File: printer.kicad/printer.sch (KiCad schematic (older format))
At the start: 35 parts, among them J1 ZX_Spectrum_128K_expansion, J2 Conn_01x08_Male, J3 Conn_01x05_Male, J4 Conn_01x04_Male, U1 SN74AHC373, U2 SN74HCT00, U3 SN74AHCT02, U4 SN74AHC373, U5 XC6206PxxxMR, U6 STM32F103C8Tx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

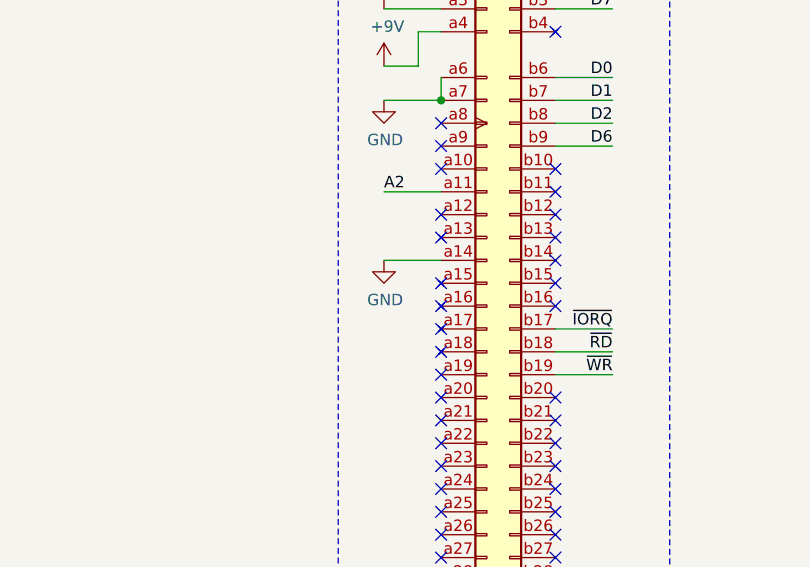
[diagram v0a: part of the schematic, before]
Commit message: Do not connect to the separate ground pin on the bus
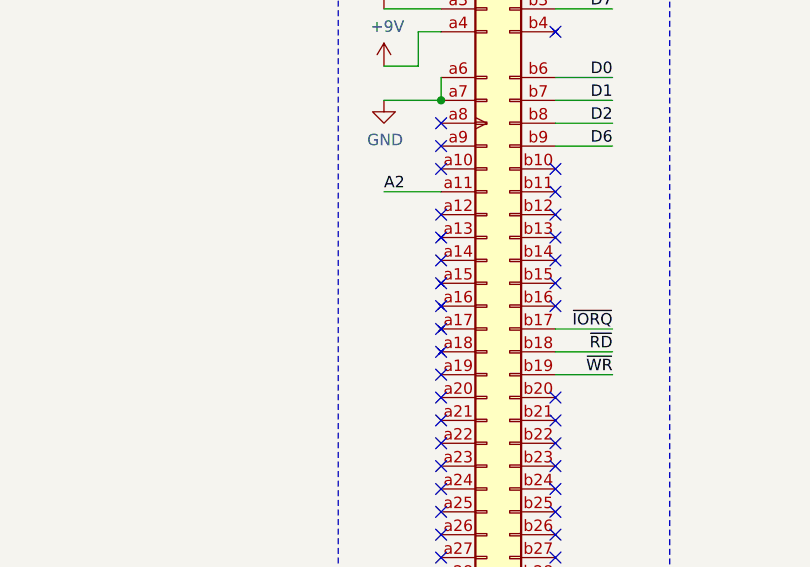
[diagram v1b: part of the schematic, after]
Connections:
- wire segments 145 -> 144
- no-connect marks 68 -> 69
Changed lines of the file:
@@
 	800  1700 1050 1700
-$Comp
-L power:GND #PWR05
-U 1 1 5E1E0363
-P 800 2400
-F 0 "#PWR05" H 800 2150 50  0001 C CNN
-F 1 "GND" H 805 2227 50  0000 C CNN
-F 2 "" H 800 2400 50  0001 C CNN
-F 3 "" H 800 2400 50  0001 C CNN
-	1    800  2400
-	1    0    0    -1
-$EndComp
-Wire Wire Line
-	800  2400 1050 2400
 $Comp
 L power:PWR_FLAG #FLG01
@@
 	1    0    0    -1
 $EndComp
+NoConn ~ 1050 2400
 $EndSCHEMATC

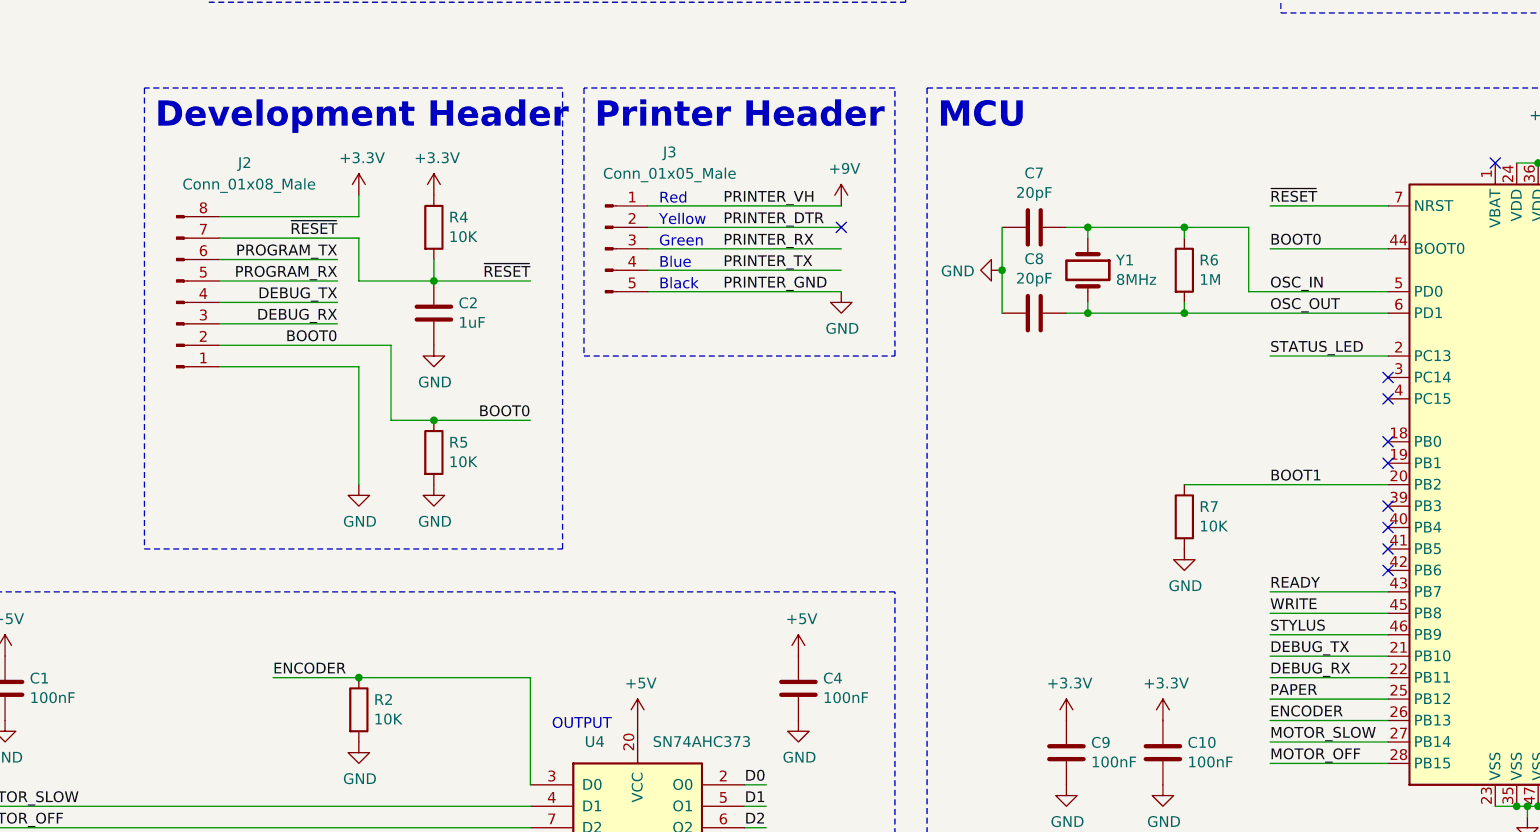
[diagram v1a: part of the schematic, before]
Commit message: Remove debug serial
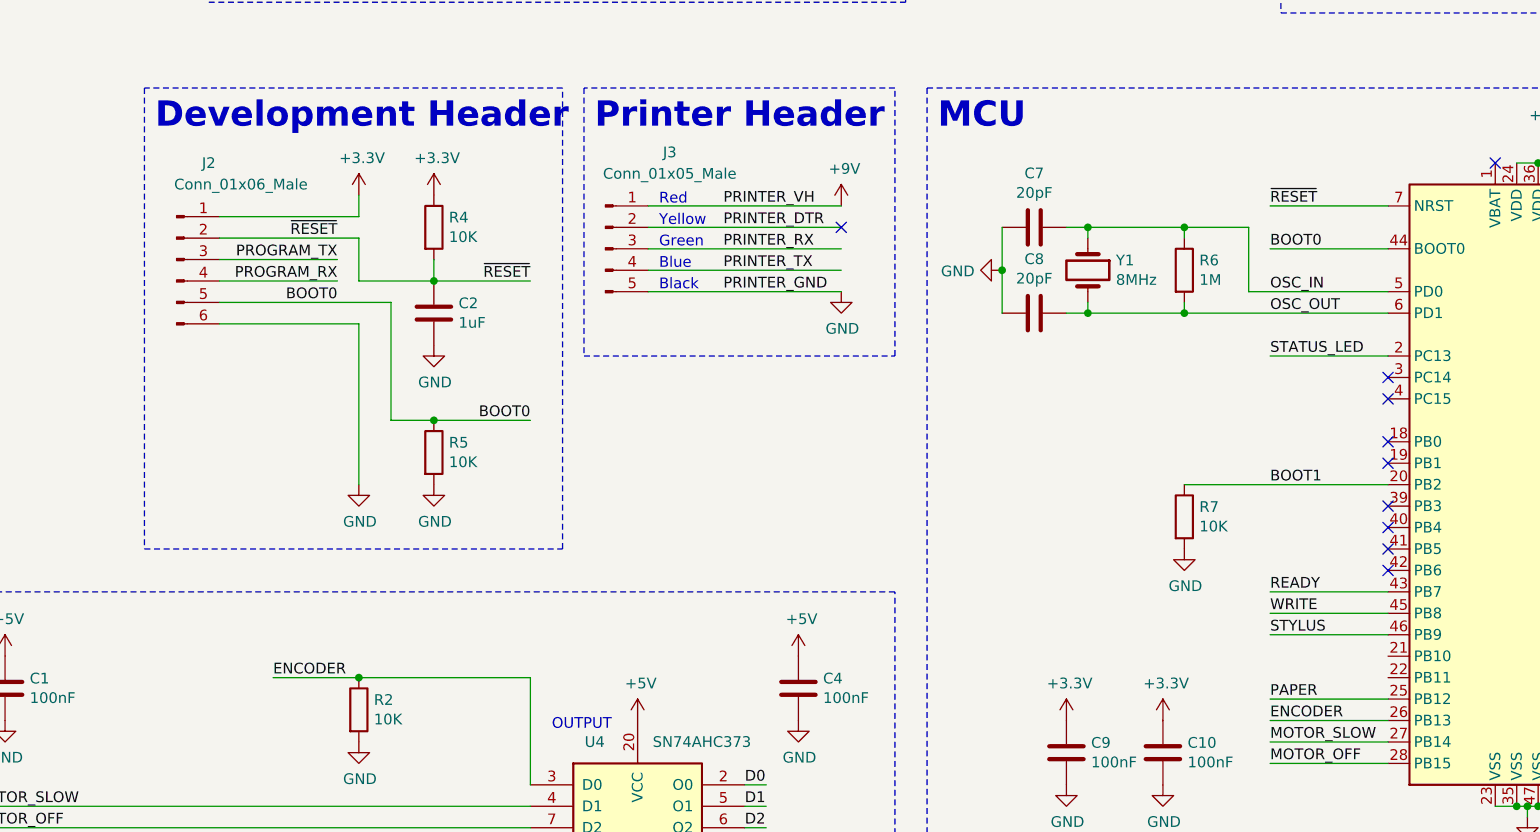
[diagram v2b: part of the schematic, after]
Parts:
- removed J2: Conn_01x08_Male, Connector_PinHeader_2.54mm:PinHeader_1x08_P2.54mm_Vertical, symbol Connector:Conn_01x08_Male
- added J2: Conn_01x06_Male, Connector_PinHeader_2.54mm:PinHeader_1x06_P2.54mm_Vertical, symbol Connector:Conn_01x06_Male
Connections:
- net labels removed: DEBUG_RX, DEBUG_TX
- wire segments 144 -> 140
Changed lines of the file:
@@
 Wire Wire Line
 	4700 5000 4700 5500
-Text Label 8150 4900 0    50   ~ 0
-DEBUG_TX
-Text Label 8150 5000 0    50   ~ 0
-DEBUG_RX
 Text Label 8150 4700 0    50   ~ 0
 WRITE
@@
 MOTOR_OFF
 Wire Wire Line
-	8150 4900 8700 4900
-Wire Wire Line
-	8150 5000 8700 5000
-Wire Wire Line
 	8150 4700 8700 4700
 Wire Wire Line
@@
 	3250 2850 3900 2850
 Wire Wire Line
-	3900 4100 3900 3550
-Wire Wire Line
 	4250 3050 4250 3150
 $Comp
@@
 	1    0    0    -1
 $EndComp
-Wire Wire Line
-	3250 3550 3900 3550
 Text Label 3800 3050 2    50   ~ 0
 PROGRAM_TX
@@
 Text Notes 6600 800  0    118  ~ 24
 MCU Power
-$Comp
-L Connector:Conn_01x08_Male J2
-U 1 1 5E996EA0
-P 3050 3250
-F 0 "J2" H 3400 2600 50  0000 R CNN
-F 1 "Conn_01x08_Male" H 3700 2700 50  0000 R CNN
-F 2 "Connector_PinHeader_2.54mm:PinHeader_1x08_P2.54mm_Vertical" H 3050 3250 50  0001 C CNN
-F 3 "~" H 3050 3250 50  0001 C CNN
-	1    3050 3250
-	1    0    0    1
-$EndComp
 Wire Wire Line
 	3900 2850 3900 2750
@@
 	3900 2950 3900 3150
 Wire Wire Line
-	4050 3800 4050 3450
-Wire Wire Line
-	4050 3450 3250 3450
-Wire Wire Line
 	3900 3150 4250 3150
 Connection ~ 4250 3150
@@
 Text Label 8150 3500 0    50   ~ 0
 STATUS_LED
-Text Label 3800 3450 2    50   ~ 0
-BOOT0
 Text Label 3800 2950 2    50   ~ 0
 ~RESET
@@
 Wire Wire Line
 	10250 1150 10800 1150
-Text Label 3800 3250 2    50   ~ 0
-DEBUG_TX
-Text Label 3800 3350 2    50   ~ 0
-DEBUG_RX
-Wire Wire Line
-	3800 3350 3250 3350
-Wire Wire Line
-	3800 3250 3250 3250
 Wire Notes Line width 10
 	9900 1750 11100 1750
@@
 $EndComp
 NoConn ~ 1050 2400
+$Comp
+L Connector:Conn_01x06_Male J2
+U 1 1 5E08EF06
+P 3050 3050
+F 0 "J2" H 3200 3500 50  0000 C CNN
+F 1 "Conn_01x06_Male" H 3350 3400 50  0000 C CNN
+F 2 "Connector_PinHeader_2.54mm:PinHeader_1x06_P2.54mm_Vertical" H 3050 3050 50  0001 C CNN
+F 3 "~" H 3050 3050 50  0001 C CNN
+	1    3050 3050
+	1    0    0    -1
+$EndComp
+Wire Wire Line
+	4050 3800 4050 3250
+Wire Wire Line
+	4050 3250 3250 3250
+Text Label 3800 3250 2    50   ~ 0
+BOOT0
+Wire Wire Line
+	3900 4100 3900 3350
+Wire Wire Line
+	3250 3350 3900 3350
 $EndSCHEMATC

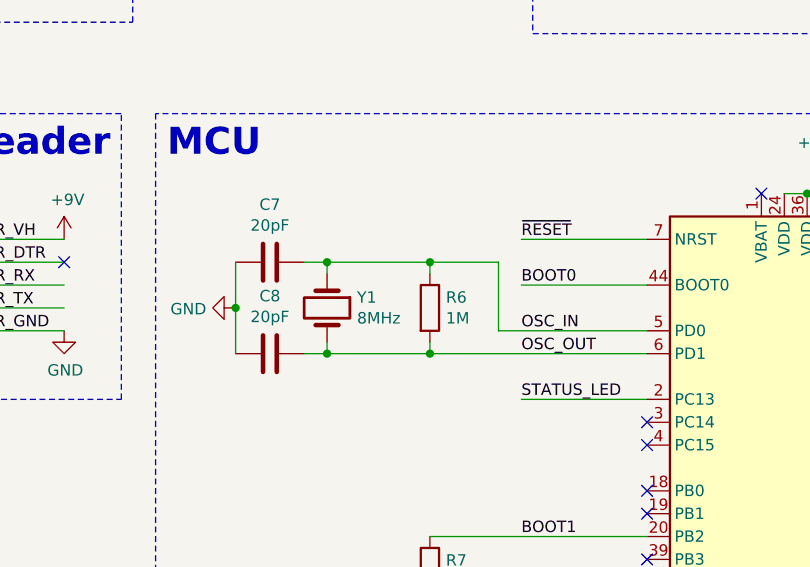
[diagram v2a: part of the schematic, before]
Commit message: Remove oscillator load resistor
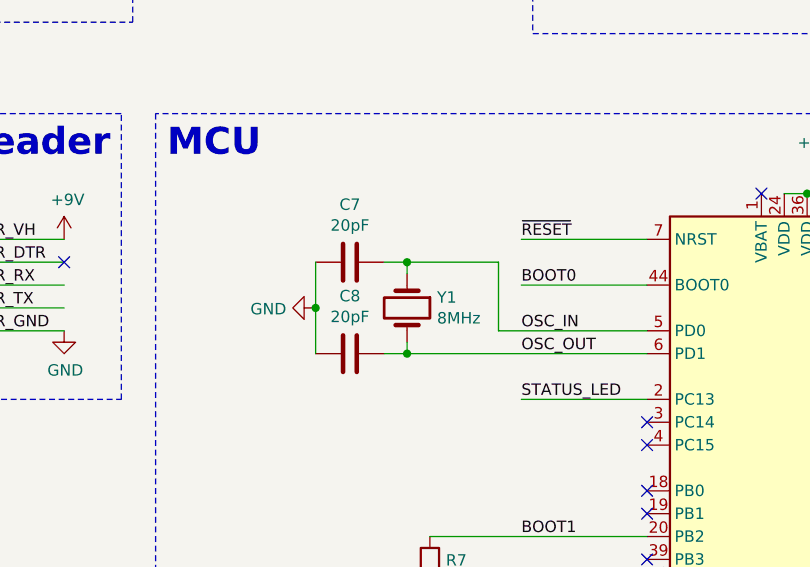
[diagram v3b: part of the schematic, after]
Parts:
- removed R6: 1M, Resistor_SMD:R_0603_1608Metric, symbol Device:R
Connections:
- wire segments 140 -> 136
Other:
- moved on the sheet: C7, C8, Y1
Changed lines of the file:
@@
 BOOT1
-$Comp
-L Device:R R6
-U 1 1 5E5F449B
-P 7750 3100
-F 0 "R6" H 7820 3146 50  0000 L CNN
-F 1 "1M" H 7820 3055 50  0000 L CNN
-F 2 "Resistor_SMD:R_0603_1608Metric" V 7680 3100 50  0001 C CNN
-F 3 "https://datasheet.lcsc.com/szlcsc/Uniroyal-Elec-0603WAF1004T5E_C22935.pdf" H 7750 3100 50  0001 C CNN
-F 4 "C22935" H 7750 3100 50  0001 C CNN "LCSC"
-	1    7750 3100
-	1    0    0    -1
-$EndComp
 $Comp
 L Device:Crystal Y1
 U 1 1 5E5F2D83
-P 7300 3100
-F 0 "Y1" V 7254 3231 50  0000 L CNN
-F 1 "8MHz" V 7345 3231 50  0000 L CNN
-F 2 "Crystal:Crystal_SMD_5032-2Pin_5.0x3.2mm" H 7300 3100 50  0001 C CNN
-F 3 "https://datasheet.lcsc.com/szlcsc/1903061615_Yangxing-Tech-X50328MSB2GI_C115962.pdf" H 7300 3100 50  0001 C CNN
-F 4 "C115962" V 7300 3100 50  0001 C CNN "LCSC"
-	1    7300 3100
+P 7650 3100
+F 0 "Y1" V 7604 3231 50  0000 L CNN
+F 1 "8MHz" V 7695 3231 50  0000 L CNN
+F 2 "Crystal:Crystal_SMD_5032-2Pin_5.0x3.2mm" H 7650 3100 50  0001 C CNN
+F 3 "https://datasheet.lcsc.com/szlcsc/1903061615_Yangxing-Tech-X50328MSB2GI_C115962.pdf" H 7650 3100 50  0001 C CNN
+F 4 "C115962" V 7650 3100 50  0001 C CNN "LCSC"
+	1    7650 3100
 	0    1    1    0
 $EndComp
 Wire Wire Line
-	7200 2900 7300 2900
-Wire Wire Line
-	7300 2900 7300 2950
-Wire Wire Line
-	7300 2900 7750 2900
-Wire Wire Line
-	7750 2900 7750 2950
-Connection ~ 7300 2900
-Wire Wire Line
-	7200 3300 7300 3300
-Wire Wire Line
-	7300 3300 7300 3250
-Wire Wire Line
-	7300 3300 7750 3300
-Wire Wire Line
-	7750 3300 7750 3250
-Connection ~ 7300 3300
-Wire Wire Line
-	6900 2900 6900 3100
-Wire Wire Line
-	8700 3300 7750 3300
-Connection ~ 7750 3300
+	7550 2900 7650 2900
+Wire Wire Line
+	7650 2900 7650 2950
+Connection ~ 7650 2900
+Wire Wire Line
+	7550 3300 7650 3300
+Wire Wire Line
+	7650 3300 7650 3250
+Connection ~ 7650 3300
+Wire Wire Line
+	7250 2900 7250 3100
 $Comp
 L power:GND #PWR034
 U 1 1 5E5E95A2
-P 6900 3100
-F 0 "#PWR034" H 6900 2850 50  0001 C CNN
-F 1 "GND" V 6905 2972 50  0000 R CNN
-F 2 "" H 6900 3100 50  0001 C CNN
-F 3 "" H 6900 3100 50  0001 C CNN
-	1    6900 3100
+P 7250 3100
+F 0 "#PWR034" H 7250 2850 50  0001 C CNN
+F 1 "GND" V 7255 2972 50  0000 R CNN
+F 2 "" H 7250 3100 50  0001 C CNN
+F 3 "" H 7250 3100 50  0001 C CNN
+	1    7250 3100
 	0    1    1    0
 $EndComp
-Connection ~ 6900 3100
-Wire Wire Line
-	6900 3100 6900 3300
+Connection ~ 7250 3100
+Wire Wire Line
+	7250 3100 7250 3300
 $Comp
 L Device:C C8
 U 1 1 5EC6FB1B
-P 7050 3300
-F 0 "C8" V 6798 3300 50  0000 C CNN
-F 1 "20pF" V 6889 3300 50  0000 C CNN
-F 2 "Capacitor_SMD:C_0603_1608Metric" H 7088 3150 50  0001 C CNN
-F 3 "https://datasheet.lcsc.com/szlcsc/Samsung-Electro-Mechanics-CL10C200JB8NNNC_C1648.pdf" H 7050 3300 50  0001 C CNN
-F 4 "C1648" H 7050 3300 50  0001 C CNN "LCSC"
-	1    7050 3300
+P 7400 3300
+F 0 "C8" V 7148 3300 50  0000 C CNN
+F 1 "20pF" V 7239 3300 50  0000 C CNN
+F 2 "Capacitor_SMD:C_0603_1608Metric" H 7438 3150 50  0001 C CNN
+F 3 "https://datasheet.lcsc.com/szlcsc/Samsung-Electro-Mechanics-CL10C200JB8NNNC_C1648.pdf" H 7400 3300 50  0001 C CNN
+F 4 "C1648" H 7400 3300 50  0001 C CNN "LCSC"
+	1    7400 3300
 	0    1    1    0
 $EndComp
@@
 L Device:C C7
 U 1 1 5ECBC64A
-P 7050 2900
-F 0 "C7" V 6798 2900 50  0000 C CNN
-F 1 "20pF" V 6889 2900 50  0000 C CNN
-F 2 "Capacitor_SMD:C_0603_1608Metric" H 7088 2750 50  0001 C CNN
-F 3 "https://datasheet.lcsc.com/szlcsc/Samsung-Electro-Mechanics-CL10C200JB8NNNC_C1648.pdf" H 7050 2900 50  0001 C CNN
-F 4 "C1648" H 7050 2900 50  0001 C CNN "LCSC"
-	1    7050 2900
+P 7400 2900
+F 0 "C7" V 7148 2900 50  0000 C CNN
+F 1 "20pF" V 7239 2900 50  0000 C CNN
+F 2 "Capacitor_SMD:C_0603_1608Metric" H 7438 2750 50  0001 C CNN
+F 3 "https://datasheet.lcsc.com/szlcsc/Samsung-Electro-Mechanics-CL10C200JB8NNNC_C1648.pdf" H 7400 2900 50  0001 C CNN
+F 4 "C1648" H 7400 2900 50  0001 C CNN "LCSC"
+	1    7400 2900
 	0    1    1    0
 $EndComp
@@
 Wire Wire Line
 	8050 3200 8050 2900
-Wire Wire Line
-	8050 2900 7750 2900
-Connection ~ 7750 2900
 Wire Notes Line width 10
 	8200 1900 9800 1900
@@
 Wire Wire Line
 	3250 3350 3900 3350
+Wire Wire Line
+	7650 2900 8050 2900
+Wire Wire Line
+	7650 3300 8700 3300
 $EndSCHEMATC
